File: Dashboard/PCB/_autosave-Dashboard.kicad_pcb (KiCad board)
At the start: 4 copper layers, 95.9 x 92.1 mm, 92 parts, among them J1 Display, J2 Conn_01x26_Female, J3 LED, J7 PROGRAMMER, SW1 SW_SPST, U1 STM32F767ZIT6, U10 24LC01, U3 MP2359DJ-LF-Z, U4 AS4C1M16S-6TCN, U5 AT25SF128A-SHB-T, U6 MP2332H, U7 MCP2561-E-SN, U8 MCP2561-E-SN, U9 ESP-12S, Y1 Crystal_GND24

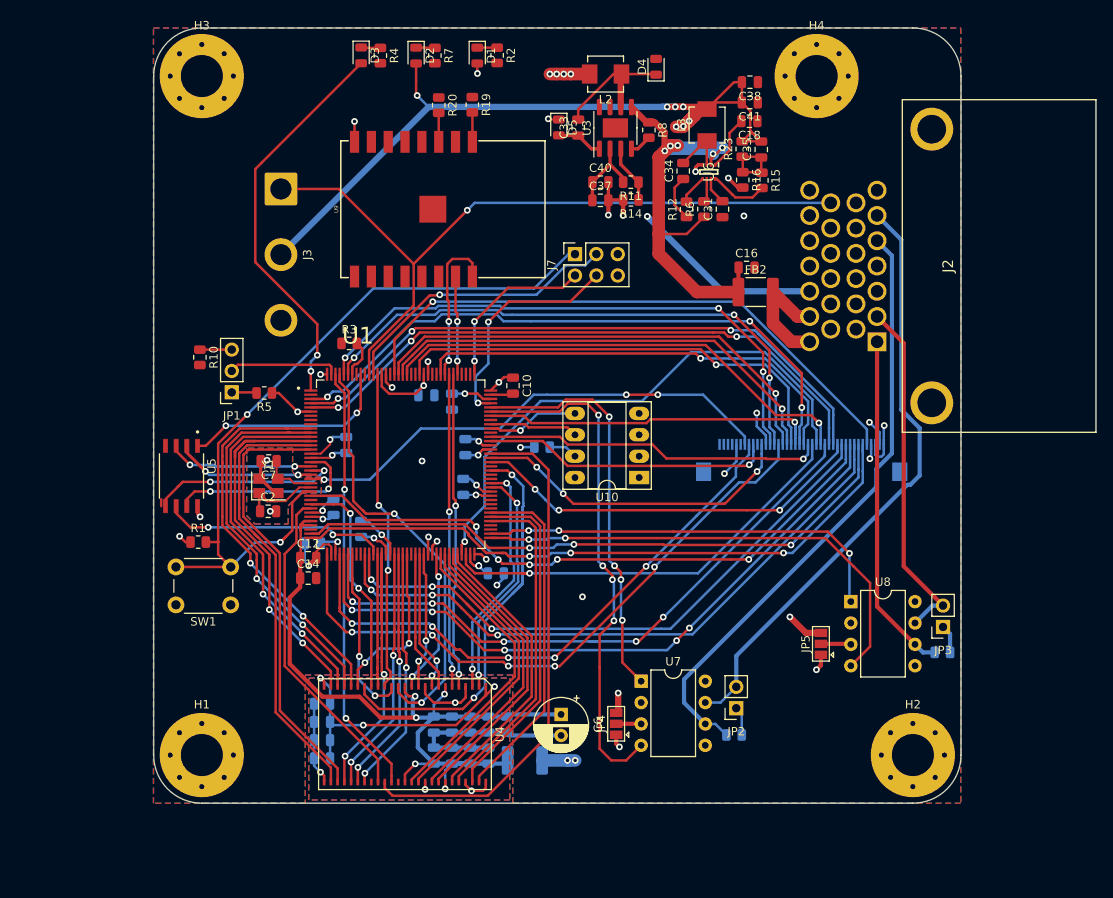
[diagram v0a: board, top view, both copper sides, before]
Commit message: Add new PCB for Dashboard (#34)
* Add usb C to board

* Add reset and pd pin to esp

* Switch footprints of converter

* Add LED Driver

* Add text to pcb

* New PCB for Dashboard
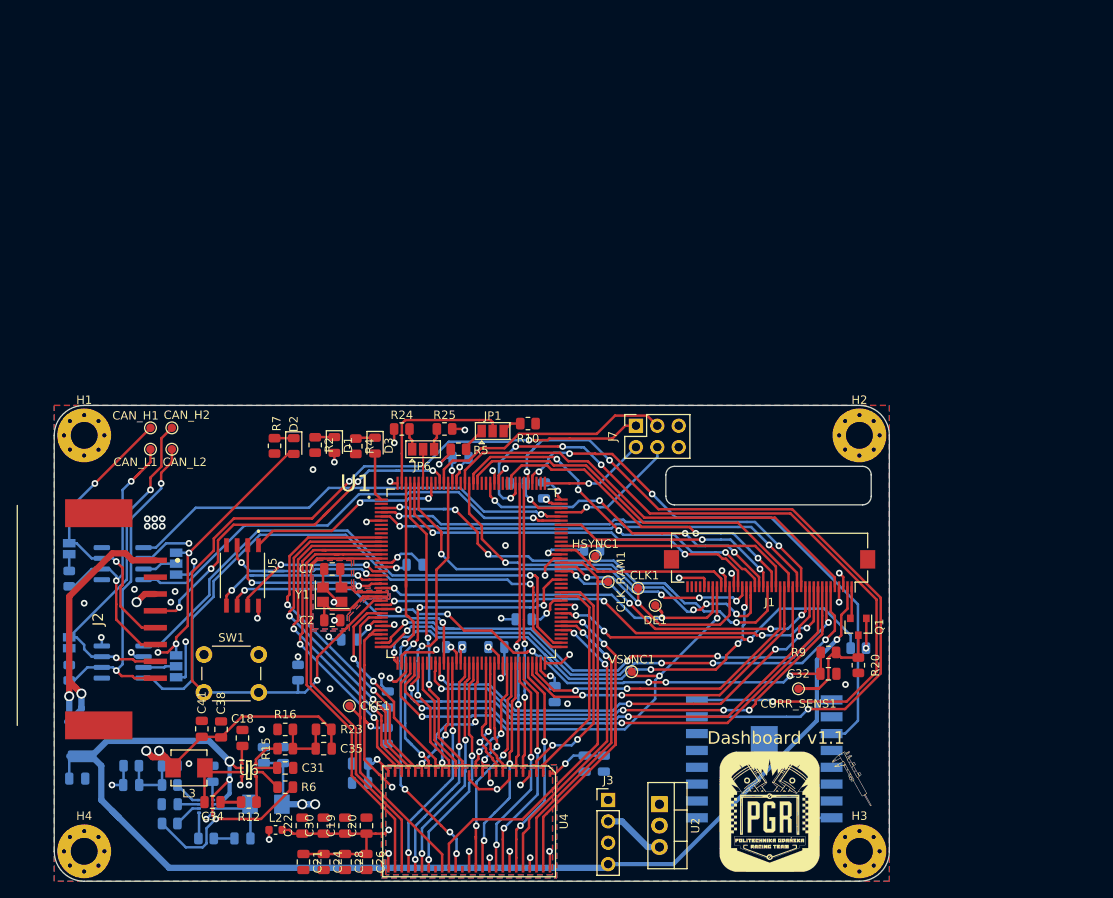
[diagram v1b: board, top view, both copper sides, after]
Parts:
- removed C4: 100nF, Capacitor_SMD:C_0805_2012Metric
- removed C6: 470uF, Capacitor_THT:CP_Radial_D6.3mm_P2.50mm
- removed D4: D_Schottky, Diode_SMD:D_0805_2012Metric
- removed D5: 1N4148, Diode_SMD:D_0805_2012Metric
- removed FB1: Ferrite_Bead, Capacitor_SMD:C_1812_4532Metric
- removed the G*** at (133.1, 71.1)
- removed R19, R21: 10k, Resistor_SMD:R_0805_2012Metric
- removed U10: 24LC01, Package_DIP:DIP-8_W7.62mm_Socket_LongPads
- added C32: 100nF, Capacitor_SMD:C_0805_2012Metric, F.Cu at (177.3, 105.9)
- added C36: 1uF, Capacitor_SMD:C_0805_2012Metric, B.Cu at (99.1, 121.4)
- added C39: 10pF, Capacitor_SMD:C_0805_2012Metric, B.Cu at (94.5, 119.1)
- added C42: 22uF, Capacitor_SMD:C_0805_2012Metric, B.Cu at (110.2, 115.6)
- added CAN_H1: TestPoint, TestPoint:TestPoint_Pad_D1.0mm, F.Cu at (96.8, 76.7)
- added CAN_H2: TestPoint, TestPoint:TestPoint_Pad_D1.0mm, F.Cu at (99.3, 76.7)
- added CAN_L1: TestPoint, TestPoint:TestPoint_Pad_D1.0mm, F.Cu at (96.8, 79.2)
- added CAN_L2: TestPoint, TestPoint:TestPoint_Pad_D1.0mm, F.Cu at (99.3, 79.2)
- added CKE1: TestPoint, TestPoint:TestPoint_Pad_D1.0mm, F.Cu at (120.4, 109.7)
- added CLK1: TestPoint, TestPoint:TestPoint_Pad_D1.0mm, F.Cu at (154.7, 95.8)
- added CLK_RAM1: TestPoint, TestPoint:TestPoint_Pad_D1.0mm, F.Cu at (151.1, 95.0)
- added CURR_SENS1: TestPoint, TestPoint:TestPoint_Pad_D1.0mm, F.Cu at (173.7, 107.7)
- added DE1: TestPoint, TestPoint:TestPoint_Pad_D1.0mm, F.Cu at (156.7, 97.8)
- added G***: LOGO, PGR_logo:logo_16x16mm, F.Cu at (170.3, 122.3)
- added G***: LOGO, PGR_logo:calliper, F.Cu at (180.1, 118.4)
- added HSYNC1: TestPoint, TestPoint:TestPoint_Pad_D1.0mm, F.Cu at (149.6, 91.9)
- added JP6: BOOT0, Jumper:SolderJumper-3_P1.3mm_Open_Pad1.0x1.5mm, F.Cu at (129.2, 79.2)
- added L1: 3.3uH, Inductor_SMD:L_Vishay_IHLP-1616, B.Cu at (110.5, 121.4)
- added Q1: Q_NMOS_GDS, Package_TO_SOT_SMD:SOT-23, F.Cu at (180.8, 100.3)
- added R13: R, Resistor_SMD:R_0805_2012Metric, B.Cu at (180.8, 102.9)
- added R24: 10k, Resistor_SMD:R_0805_2012Metric, F.Cu at (126.6, 76.8)
- added R25: 10k, Resistor_SMD:R_0805_2012Metric, F.Cu at (131.7, 76.8)
- added R26: 40.2k, Resistor_SMD:R_0805_2012Metric, B.Cu at (94.5, 116.8)
- added R9: R, Resistor_SMD:R_0805_2012Metric, F.Cu at (177.3, 103.4)
- added U2: IFX27001TFV33, Package_TO_SOT_THT:TO-220-3_Vertical, F.Cu at (157.2, 121.4)
- added VSYNC1: TestPoint, TestPoint:TestPoint_Pad_D1.0mm, F.Cu at (153.9, 105.7)
- C10, C12, C14, C16, FB2, JP4, JP5, R1, U9: moved to B.Cu
- C19, C20, C21, C22, C24, C26, C28, C30, J1: moved to F.Cu
- C33: value 10nF -> 1uF; moved to B.Cu
- C37: value 10uF -> 1uF; moved to B.Cu
- C40: value 10uF -> 22uF; moved to B.Cu
- H1, H2, H3, H4: footprint MountingHole:MountingHole_5mm_Pad_Via -> MountingHole:MountingHole_3.2mm_M3_Pad_Via
- J2: value Conn_01x26_Female -> 34912-6080; footprint Konektor:64734231 -> DashboardConnector:349126080
- J3: value LED -> Conn_01x04_Female; footprint Connector_Wire:SolderWire-2sqmm_1x03_P7.8mm_D2mm_OD3.9mm -> Connector_PinHeader_2.54mm:PinHeader_1x04_P2.54mm_Vertical
- JP1: footprint Connector_PinSocket_2.54mm:PinSocket_1x03_P2.54mm_Vertical -> Jumper:SolderJumper-3_P1.3mm_Open_Pad1.0x1.5mm
- JP2, JP3: footprint Connector_PinSocket_2.54mm:PinSocket_1x02_P2.54mm_Vertical -> Jumper:SolderJumper-2_P1.3mm_Open_Pad1.0x1.5mm; moved to B.Cu
- L2: value 10uH -> 39nH; footprint Inductor_SMD:L_Vishay_IHLP-1616 -> Inductor_SMD:L_0603_1608Metric
- R11: value R -> 20k; moved to B.Cu
- R14: value R -> 13k; moved to B.Cu
- R20: value 10k -> 1R
- R3: value 10k -> 100k; moved to B.Cu
- R8: value 100k -> R; moved to B.Cu
- U3: value MP2359DJ-LF-Z -> MP2332H; footprint Package_SO:SOIC-8-1EP_3.9x4.9mm_P1.27mm_EP2.29x3mm -> SOT-583:SOTFL50P160X60-8N; moved to B.Cu
- U7, U8: footprint Package_DIP:DIP-8_W7.62mm -> Package_SO:SOIC-8_3.9x4.9mm_P1.27mm; moved to B.Cu
- moved H4 126.7 mm to (88.9, 127.0)
- moved H3 120.7 mm to (181.0, 127.0)
- moved JP3 103.8 mm to (87.1, 102.2), turned to 90 degrees
- moved R18 103.7 mm to (87.1, 105.8), turned to 270 degrees
- moved C16 100.0 mm to (88.1, 118.4)
- moved C38 99.3 mm to (105.2, 112.5), turned to 270 degrees
- moved R8 99.2 mm to (103.4, 125.5), turned to 180 degrees
- moved C41 98.8 mm to (102.9, 112.5), turned to 270 degrees
- moved J2 98.2 mm to (90.6, 99.4), turned to 270 degrees
- moved L3 98.1 mm to (101.3, 117.1), turned to 180 degrees
- moved L2 98.0 mm to (111.6, 124.5), turned to 0 degrees
- moved FB2 96.0 mm to (88.6, 113.7), turned to 90 degrees
- moved C18 94.8 mm to (107.7, 113.5), turned to 270 degrees
- moved U3 94.1 mm to (103.4, 121.7), turned to 180 degrees
- moved C34 93.5 mm to (104.1, 121.2), turned to 180 degrees
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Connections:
- net Net-(U1-Pad111) renamed ESP_RESET
- net Net-(U1-Pad75) renamed USB_OTG_DM
- net Net-(U1-Pad76) renamed USB_OTG_DP
- C33 pad 1: Net-(C33-Pad1) -> GND
- C37 pad 1: GND -> Net-(C37-Pad1)
- C37 pad 2: +3V3 -> Net-(C37-Pad2)
- J1 pad 1: GND -> DISPLAY_LED-
- J1 pad 2: +5V -> +12L
- J1 pad 31: /DISPLAY_EN -> +3V3
- J2 pad 1: CAN_L2 -> +12V
- J2 pad 2: CAN_H2 -> GND
- J2 pad 3: Net-(J2-Pad3) -> +5V
- J2 pad 4: Net-(J2-Pad4) -> LED_DATA
- J2 pad 5: CAN_L1 -> CAN_H1
- J2 pad 6: CAN_H1 -> CAN_L1
- J2 pad 7: Net-(J2-Pad7) -> CAN_H2
- J2 pad 8: Net-(J2-Pad8) -> CAN_L2
- J3 pad 1: LED_DATA -> GND
- J7 pad 5: GND -> Net-(D7-Pad2)
- L2 pad 1: Net-(C33-Pad2) -> +3V3
- L2 pad 2: +3V3 -> +3.3VA
- R11 pad 1: Net-(R11-Pad1) -> Net-(C39-Pad1)
- R11 pad 2: GND -> Net-(R11-Pad2)
- R14 pad 1: Net-(R11-Pad1) -> Net-(C39-Pad1)
- R14 pad 2: +3V3 -> GND
- R20 pad 2: Net-(R20-Pad2) -> GND
- R3 pad 1: GND -> +12L
- R8 pad 1: +12L -> Net-(C37-Pad1)
- U1 pad 112: Net-(U1-Pad112) -> ESP_EN
- U1 pad 138: Net-(R3-Pad2) -> Net-(JP6-Pad2)
- U1 pad 27: Net-(U1-Pad27) -> LED_CURRENT_SENSE
- U1 pad 81: Net-(U1-Pad81) -> LED_PWM
- U3 pad 1: Net-(C33-Pad1) -> Net-(C33-Pad2)
- U3 pad 2: GND -> +12L
- U3 pad 3: Net-(R11-Pad1) -> Net-(C37-Pad2)
- U3 pad 4: Net-(R8-Pad2) -> GND
- U3 pad 5: +12L -> Net-(R8-Pad2)
- U3 pad 6: Net-(C33-Pad2) -> Net-(R3-Pad2)
- U3 pad 7: (no net) -> Net-(C36-Pad2)
- U3 pad 8: (no net) -> Net-(R11-Pad2)
- U9 pad 3: Net-(R20-Pad2) -> ESP_EN
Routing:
- net +12L: track 59.8 -> 177.8 mm, vias 5 -> 4
- net +5V: track 255.2 -> 167.5 mm, vias 11 -> 6
- net ESP_UART_RX: track 11.7 -> 86.8 mm, vias 2 -> 3
- net ESP_UART_TX: track 18.4 -> 91.9 mm, vias 2 -> 5
- net ESP_EN: track 0.00 -> 66.0 mm, vias 0 -> 3
- net LED_CURRENT_SENSE: track 0.00 -> 59.3 mm, vias 0 -> 6
- net GND: track 122.4 -> 77.6 mm, vias 25 -> 49
- net LED_DATA: track 87.3 -> 44.7 mm, vias 1 -> 4
- net SIGNAL_LED: track 47.5 -> 5.78 mm, vias 2 -> 0
- net LED_PWM: track 0.00 -> 40.1 mm, vias 0 -> 3
- net CAN_H1: track 71.8 -> 35.1 mm, vias 0 -> 2
- net CAN_L1: track 72.4 -> 35.8 mm, vias 0 -> 2
- net +3.3VA: track 91.8 -> 63.8 mm, vias 5 -> 6
- net /LTDC_G4: track 64.6 -> 40.9 mm, vias 1 -> 2
- net /LTDC_B7: track 67.7 -> 46.8 mm, vias 3 -> 2
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- added copper zone on In1.Cu, net +3.3VA
- added copper zone on In1.Cu, net +3V3
- added copper zone on In2.Cu, net GND
- removed copper zone on In2.Cu, net +3V3
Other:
- board size 95.9 x 92.1 mm -> 99.2 x 56.5 mm
- board text added: "Dashboard v1.1"
- board text added: "M. NADARZYŃSKI"
- board text removed: "M. NADARZYNSKI"
